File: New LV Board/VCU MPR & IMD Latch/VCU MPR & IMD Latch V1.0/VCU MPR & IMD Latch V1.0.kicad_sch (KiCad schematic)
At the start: 15 parts, among them J1 691137710002, J2 B12B-PH-K-S, J4 691137710002, K1 ALF1PF12, K2 AHES4291, SW1 Test Reset IMD

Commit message: VCU MPR and IMP Latch
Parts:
- removed K2: AHES4291, motorsports:AHES4_PAN, symbol Relay:AHES4291
- added K2, K3, K4: A161CS12VDC.64, A161CS12VDC.64:RELAY_A161CS12VDC.64, symbol New_Library:A161CS12VDC.64
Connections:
- net Vs is gone; now on an unnamed net: J2.4
- net at D4.2 (A), J2.5: now also K4.NC
- net at D1.1 (K), D2.1 (K), D3.1 (K)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: now also K2.A2, K3.A2, K3.NO, K4.A2
- net at J2.8, J4.1: now also K2.NO; no longer TP2.1
- net at J4.2: now also K2.COM
- net at J2.2, R3.1, SW1.2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: now also K3.COM, K4.COM; no longer J2.6
- net GND: no longer names the net of D1.2 (A), D2.2 (A), J2.7, R1.1, R2.1, R3.2
- net GND: now also TP2.1; no longer D3.2 (A)
- new net: D3.2 (A), J2.6, K2.A1, K3.A1, K4.A1
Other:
- note removed: "AMS LED +"
- note removed: "To Safety Loop"
- moved on the sheet: D1, D2, D3, D4, J4, R1, R2, R3, SW1, TP1, TP2

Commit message: Opening files forcing me to commit
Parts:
- K2, K3, K4: footprint A161CS12VDC.64:RELAY_A161CS12VDC.64 -> Library:RELAY_A161CS12VDC.64
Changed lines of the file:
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@@
 			)
 		)
-		(property "Footprint" "A161CS12VDC.64:RELAY_A161CS12VDC.64"
+		(property "Footprint" "Library:RELAY_A161CS12VDC.64"
 			(at 68.58 137.16 0)
 			(effects
@@
 			)
 		)
-		(property "Footprint" "A161CS12VDC.64:RELAY_A161CS12VDC.64"
+		(property "Footprint" "Library:RELAY_A161CS12VDC.64"
 			(at 68.58 110.49 0)
 			(effects
@@
 			)
 		)
-		(property "Footprint" "A161CS12VDC.64:RELAY_A161CS12VDC.64"
+		(property "Footprint" "Library:RELAY_A161CS12VDC.64"
 			(at 68.58 83.82 0)
 			(effects

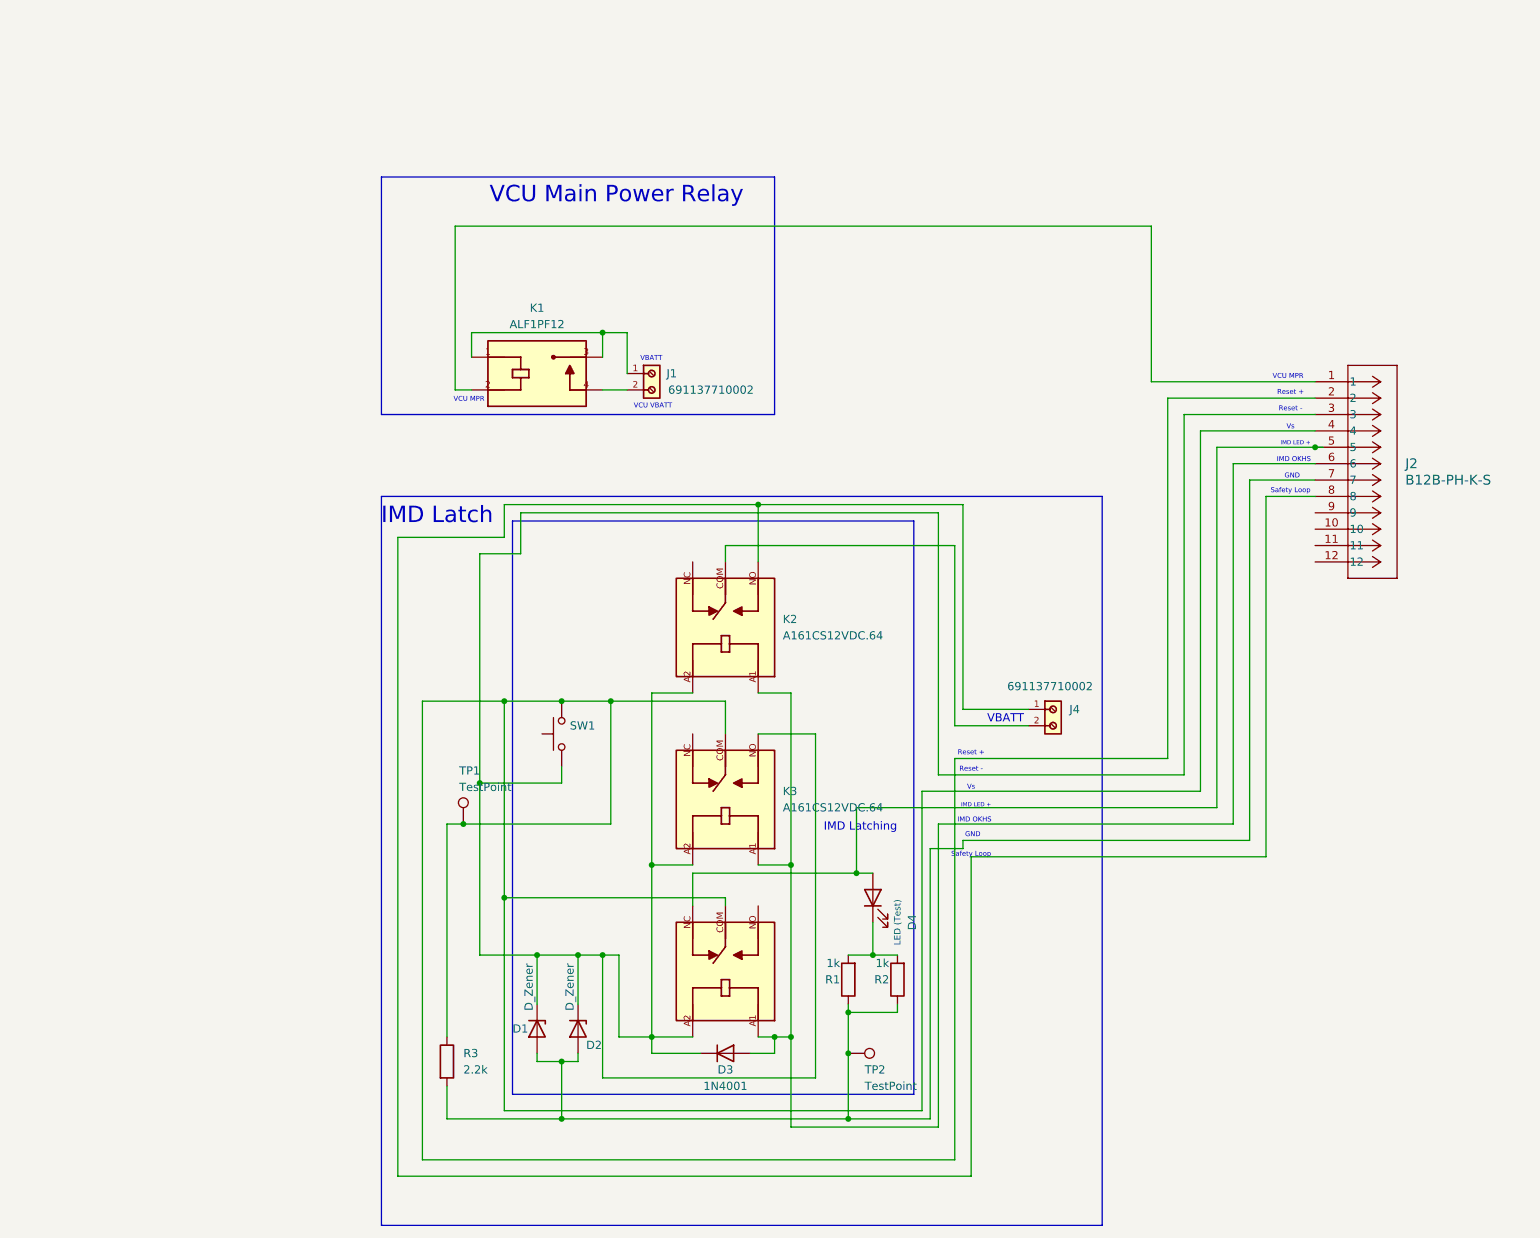
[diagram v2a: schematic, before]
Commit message: Changed file name of VCU Throttle Latching to Throttle Latching Module, attempt to make VCU MPR & IMD Latch into IMD Latch & AMS Latch.
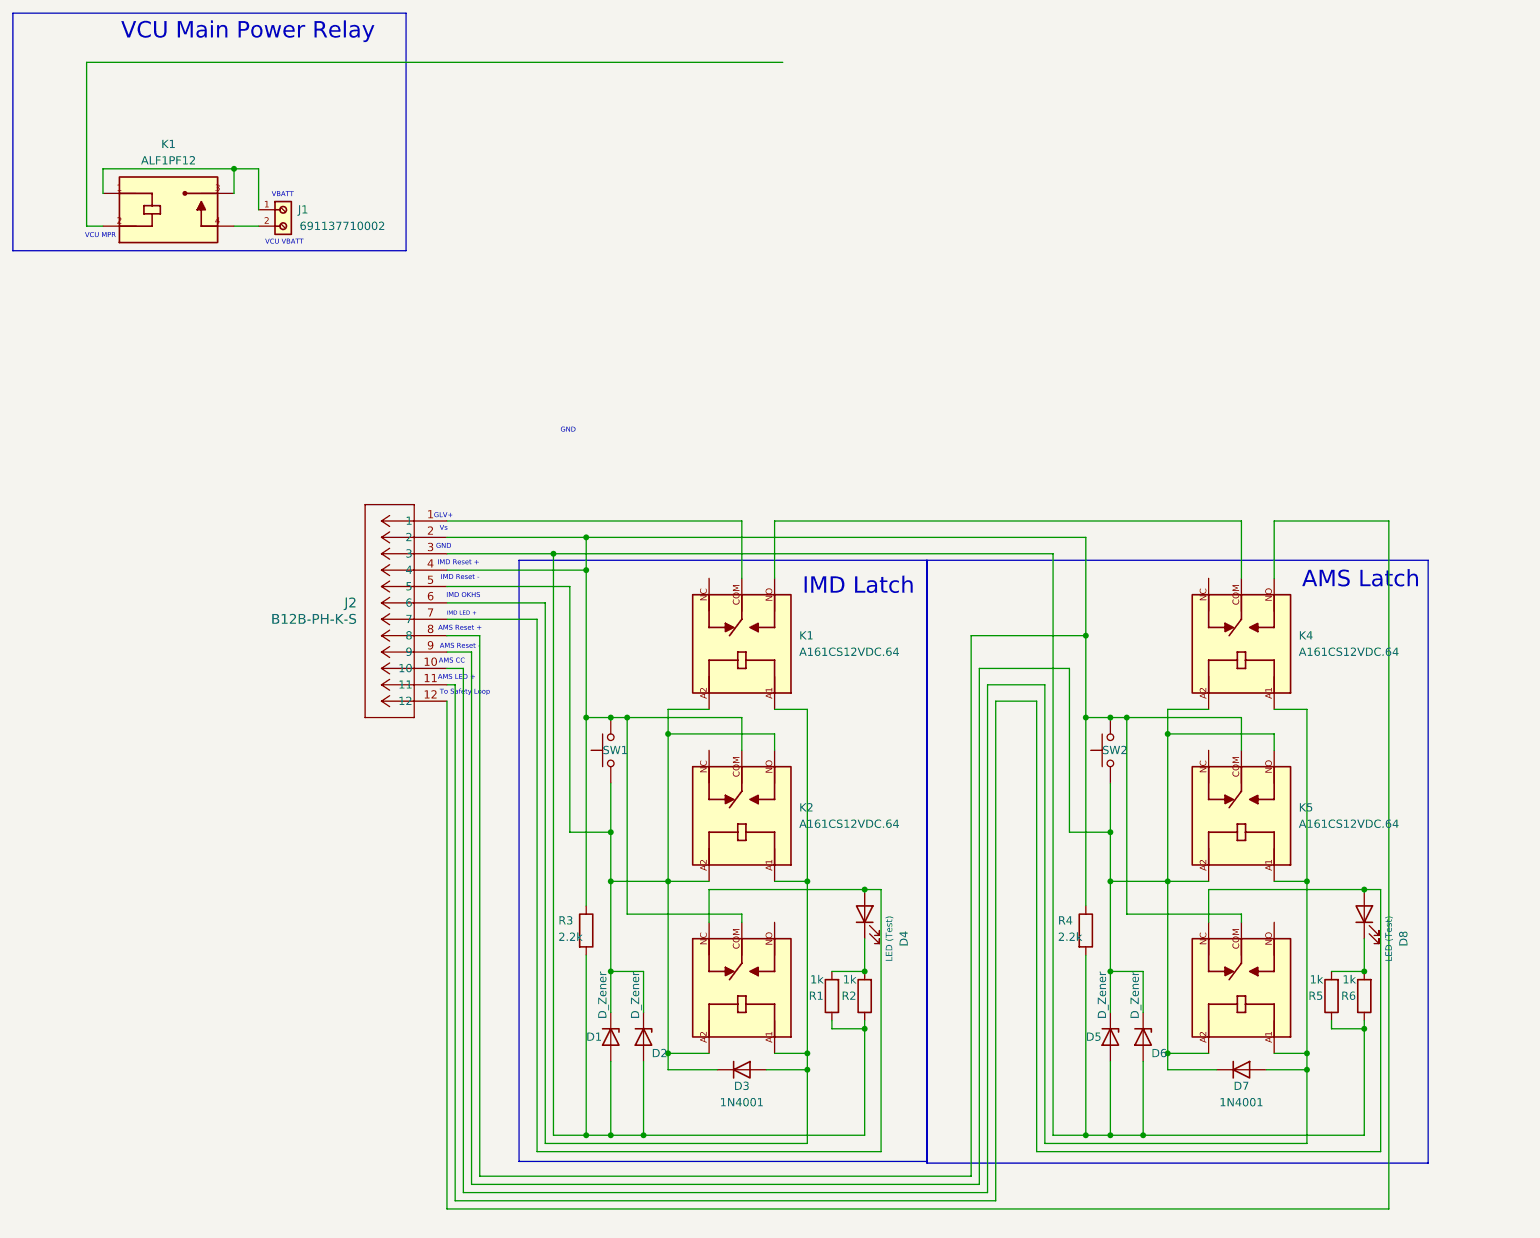
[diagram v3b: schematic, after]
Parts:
- removed J4: 691137710002, motorsports:691137710002, symbol 691137710002:691137710002
- removed TP1, TP2: TestPoint, TestPoint:TestPoint_Loop_D2.60mm_Drill1.6mm_Beaded, symbol Connector:TestPoint
- added D5, D6: D_Zener, motorsports:STA_RMCF0603_STP-L, symbol Device:D_Zener
- added D7: 1N4001, Diode_THT:D_DO-41_SOD81_P10.16mm_Horizontal, symbol Diode:1N4001
- added D8: LED (Test), motorsports:LED_AP3216SYD_KNB, symbol Device:LED
- added K4, K5, K6: A161CS12VDC.64, Library:RELAY_A161CS12VDC.64, symbol New_Library:A161CS12VDC.64
- added R4: 2.2k, Resistor_THT:R_Axial_DIN0204_L3.6mm_D1.6mm_P7.62mm_Horizontal, symbol Device:R
- added R5, R6: 1k, Resistor_THT:R_Axial_DIN0204_L3.6mm_D1.6mm_P7.62mm_Horizontal, symbol Device:R
- added SW2: Test Reset IMD, motorsports:pushButton, symbol Switch:SW_Push
- renumbered K2 to K1, K3 to K2, K4 to K3
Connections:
- net at D4.2 (A), K3.NC: now also J2.7; no longer J2.5
- net at D1.1 (K), D2.1 (K), D3.1 (K)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: now also J2.5; no longer J2.3
- net at J2.2, J2.4, K2.COM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: now also J2.8, K5.COM, K6.COM, R4.1, SW2.2
- net at K1.NO: now also K4.COM; no longer J2.8
- net at K1.COM: now also J2.1
- net at D1.2 (A), D2.2 (A), R1.1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: now also J2.3, D5.2 (A), D6.2 (A), R4.2, R5.1, R6.1; no longer J2.7
- net at K1.2: no longer J2.1
- net at J2.10: now also D7.2 (A), K4.A1, K5.A1, K6.A1
- net at J2.11: now also D8.2 (A), K6.NC
- net at J2.12: now also K4.NO
- net at J2.9: now also D5.1 (K), D6.1 (K), D7.1 (K), K4.A2, K5.A2, K5.NO, K6.A2, SW2.1
- new net: D8.1 (K), R5.2, R6.2
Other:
- note added: "AMS CC"
- note added: "AMS LED +"
- note added: "AMS Latch"
- note added: "AMS Reset +"
- note added: "AMS Reset -"
- note added: "GLV+"
- note added: "IMD Reset +"
- note added: "IMD Reset -"
- note added: "To Safety Loop"
- note removed: "IMD Latching"
- note removed: "Reset +"
- note removed: "Reset -"
- note removed: "Safety Loop"
- moved on the sheet: D1, D2, D3, D4, J1, J2, K1, K2, R1, R2, R3, SW1

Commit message: AMS and IMD Latch combination
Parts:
- removed J1: 691137710002, motorsports:691137710002, symbol 691137710002:691137710002
- removed K1: ALF1PF12, motorsports:RELAY_ALF1PF12, symbol ALF1PF12:ALF1PF12
- removed R1, R5: 1k, Resistor_THT:R_Axial_DIN0204_L3.6mm_D1.6mm_P7.62mm_Horizontal, symbol Device:R
- D1, D2, D5, D6: value D_Zener -> 1N4743A; footprint motorsports:STA_RMCF0603_STP-L -> Diode_THT:D_DO-41_SOD81_P3.81mm_Vertical_AnodeUp
- D4, D8: footprint motorsports:LED_AP3216SYD_KNB -> LED_THT:LED_D3.0mm
- J2: footprint CONN12_B12B-PH_JST -> Connector_JST:JST_PH_B12B-PH-K_1x12_P2.00mm_Vertical
- R1: renamed from R2; value 1k -> 680; footprint Resistor_THT:R_Axial_DIN0204_L3.6mm_D1.6mm_P7.62mm_Horizontal -> Resistor_THT:R_Axial_DIN0207_L6.3mm_D2.5mm_P2.54mm_Vertical
- R2: renamed from R6; value 1k -> 680; footprint Resistor_THT:R_Axial_DIN0204_L3.6mm_D1.6mm_P7.62mm_Horizontal -> Resistor_THT:R_Axial_DIN0207_L6.3mm_D2.5mm_P2.54mm_Vertical
- R3, R4: footprint Resistor_THT:R_Axial_DIN0204_L3.6mm_D1.6mm_P7.62mm_Horizontal -> Resistor_THT:R_Axial_DIN0207_L6.3mm_D2.5mm_P2.54mm_Vertical
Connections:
- net at D3.2 (A), K1.A1, K2.A1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: now also D1.2 (A), D2.2 (A), D5.2 (A), D6.2 (A), J2.3, R1.1, R2.1, R3.2, R4.2; no longer J2.6
- net at J2.2, J2.8, K5.COM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: no longer J2.4, K2.COM, K3.COM, R3.1, SW1.2
- new net: J2.4, J2.6, K2.COM, K3.COM, R3.1, SW1.2
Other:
- note removed: "VBATT"
- note removed: "VCU MPR"
- note removed: "VCU Main Power Relay"
- note removed: "VCU VBATT"
